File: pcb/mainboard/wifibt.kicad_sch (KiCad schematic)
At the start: 11 parts, among them U901 RTL8723BS

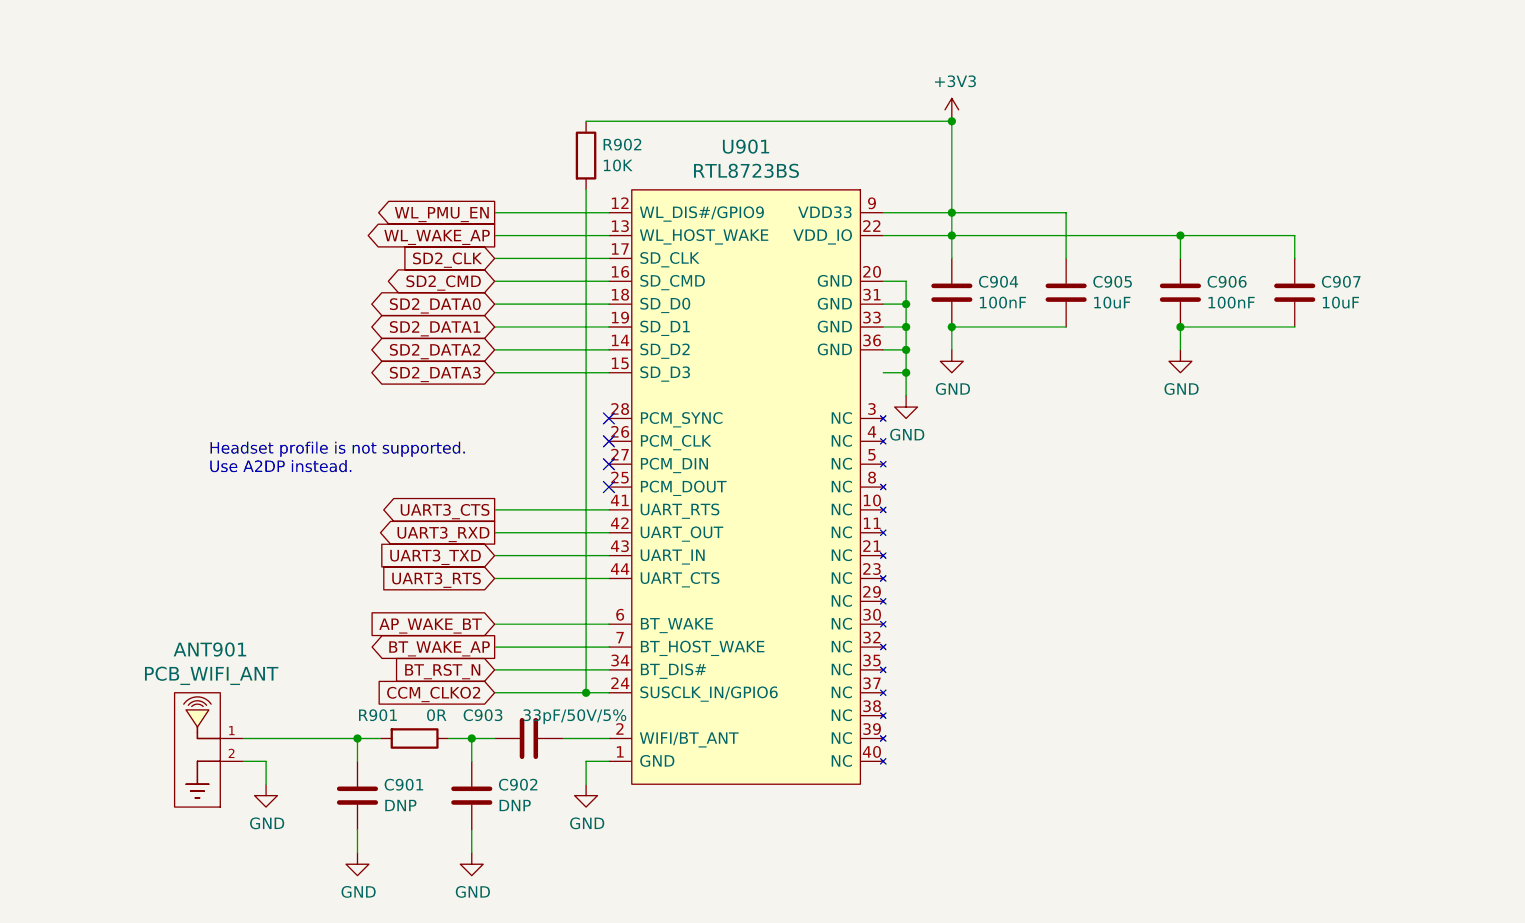
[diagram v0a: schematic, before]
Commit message: pcb: preliminary r0p1 schematics
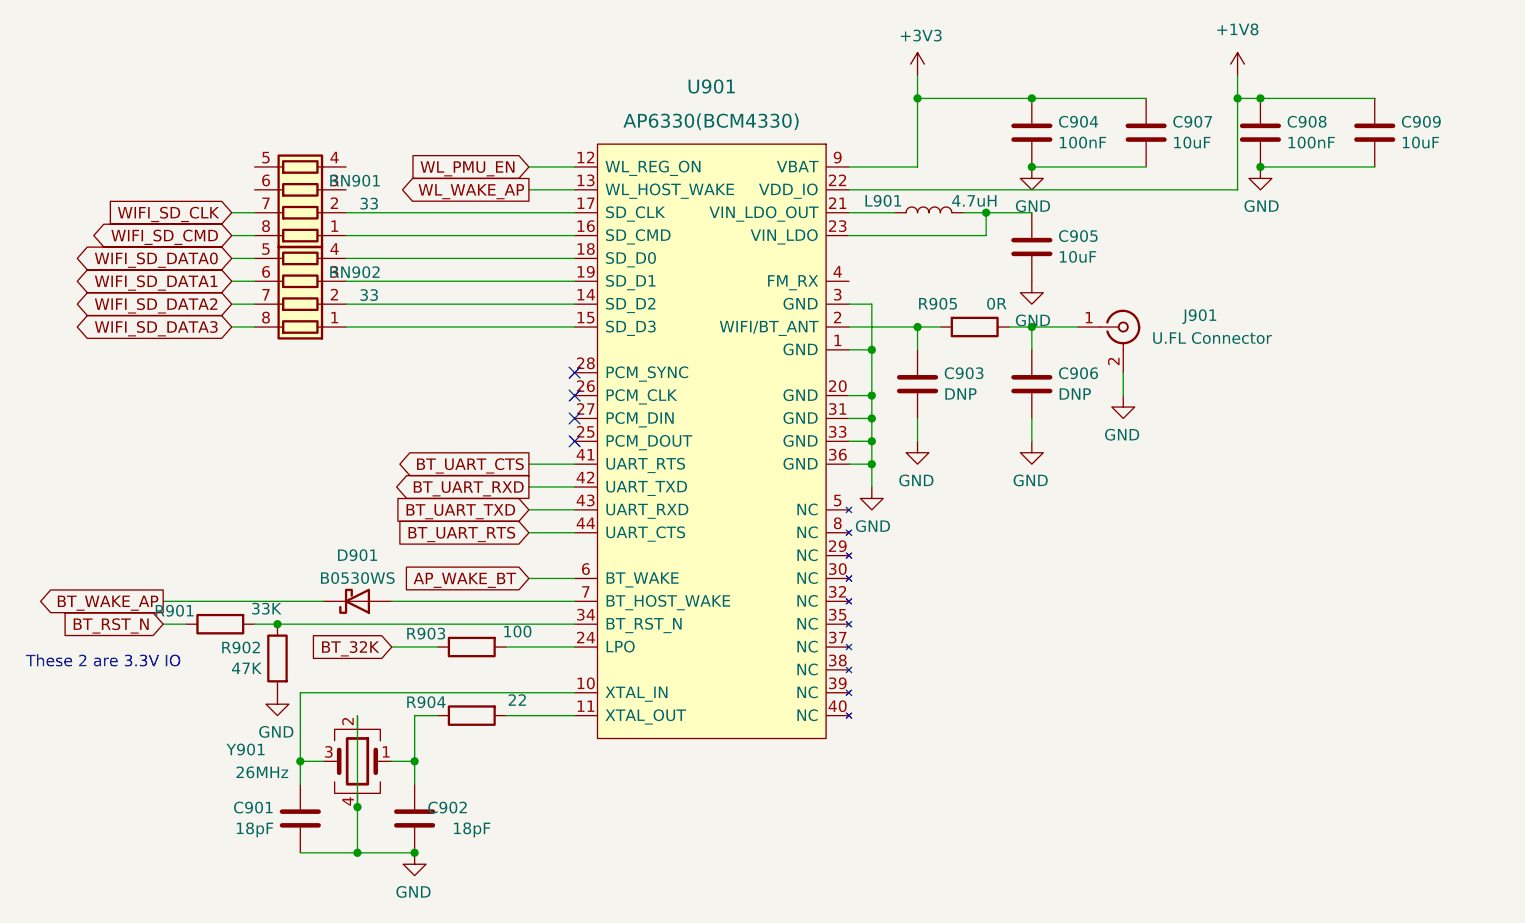
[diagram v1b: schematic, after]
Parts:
- removed ANT901: PCB_WIFI_ANT, footprints:bt_antenna_1ant_2gnd, symbol symbols:WIFI_ANT_ESP8266
- removed U901: RTL8723BS, footprints:RL-SM02BD(RTL8723BS), symbol symbols:RTL8723BS
- added C908: 100nF, Capacitor_SMD:C_0402_1005Metric, symbol Device:C
- added C909: 10uF, Capacitor_SMD:C_0603_1608Metric, symbol Device:C
- added D901: B0530WS, Diode_SMD:D_SOD-323, symbol Device:D_Schottky
- added J901: U.FL Connector, Connector_Coaxial:U.FL_Molex_MCRF_73412-0110_Vertical, symbol Connector:Conn_Coaxial
- added L901: 4.7uH, footprints:L_1212, symbol Device:L
- added R903: 100, Resistor_SMD:R_0402_1005Metric, symbol Device:R
- added R904: 22, Resistor_SMD:R_0402_1005Metric, symbol Device:R
- added R905: 0R, Resistor_SMD:R_0402_1005Metric, symbol Device:R
- added RN901, RN902: 33, Resistor_SMD:R_Array_Convex_4x0402, symbol Device:R_Pack04
- added U901: AP6330(BCM4330), footprints:RL-SM02BD(RTL8723BS), symbol symbols:AP6330(BCM4330)
- added Y901: 26MHz, Oscillator:Oscillator_SMD_Abracon_ASE-4Pin_3.2x2.5mm, symbol Device:Crystal_GND24
- C901, C902: value DNP -> 18pF
- C903: value 33pF/50V/5% -> DNP
- C906: value 100nF -> DNP
- R901: value 0R -> 33K
- R902: value 10K -> 47K
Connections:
- net CCM_CLKO2 is gone; now on net GND: R902.2
- net +3V3: now also U901.9 (VBAT); no longer C905.1, C906.1, R902.1
- net AP_WAKE_BT: now also U901.6 (BT_WAKE)
- net BT_RST_N: now also R901.1
- net BT_WAKE_AP: now also D901.1 (K)
- net GND: now also C901.2, C902.2, C903.1, C906.1, C908.2, C909.2, J901.2 (Ext), U901.1 (GND), U901.20 (GND), U901.3 (GND), U901.31 (GND), U901.33 (GND), U901.36 (GND), Y901.2, Y901.4; no longer C901.1, C902.1, C906.2
- net WL_PMU_EN: now also U901.12 (WL_REG_ON)
- net WL_WAKE_AP: now also U901.13 (WL_HOST_WAKE)
- net at R901.2: now also R902.1, U901.34 (BT_RST_N); no longer C901.2
- new net: RN902.1 (R1.1), U901.15 (SD_D3)
- new net: RN902.2 (R2.1), U901.14 (SD_D2)
- new net: RN902.3 (R3.1), U901.19 (SD_D1)
- new net: RN902.4 (R4.1), U901.18 (SD_D0)
- new net: C906.2, J901.1 (In), R905.1
- new net: C905.1, L901.2, U901.23 (VIN_LDO)
- new net: RN901.1 (R1.1), U901.16 (SD_CMD)
- new net: RN901.2 (R2.1), U901.17 (SD_CLK)
- new net: L901.1, U901.21 (VIN_LDO_OUT)
- new net: D901.2 (A), U901.7 (BT_HOST_WAKE)
- new net: C901.1, U901.10 (XTAL_IN), Y901.3
- new net: R903.2, U901.24 (LPO)
- new net: C902.1, R904.1, Y901.1
- new net: C903.2, R905.2, U901.2 (WIFI/BT_ANT)
- new net: R904.2, U901.11 (XTAL_OUT)
- new net +1V8: C908.1, C909.1, U901.22 (VDD_IO)
- new net BT_32K: R903.1
- new net BT_UART_CTS: U901.41 (UART_RTS)
- new net BT_UART_RTS: U901.44 (UART_CTS)
- new net BT_UART_RXD: U901.42 (UART_TXD)
- new net BT_UART_TXD: U901.43 (UART_RXD)
- new net WIFI_SD_CLK: RN901.7 (R2.2)
- new net WIFI_SD_CMD: RN901.8 (R1.2)
- new net WIFI_SD_DATA0: RN902.5 (R4.2)
- new net WIFI_SD_DATA1: RN902.6 (R3.2)
- new net WIFI_SD_DATA2: RN902.7 (R2.2)
- new net WIFI_SD_DATA3: RN902.8 (R1.2)
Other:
- note added: "These 2 are 3.3V IO"
- note removed: "Headset profile is not supported. Use A2DP instead."
- company: Copyright EI-2030 2021. / Engineer: Wenting Zhang -> Copyright Modos 2021. / Engineer: Wenting Zhang

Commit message: pcb: initial placement for mb
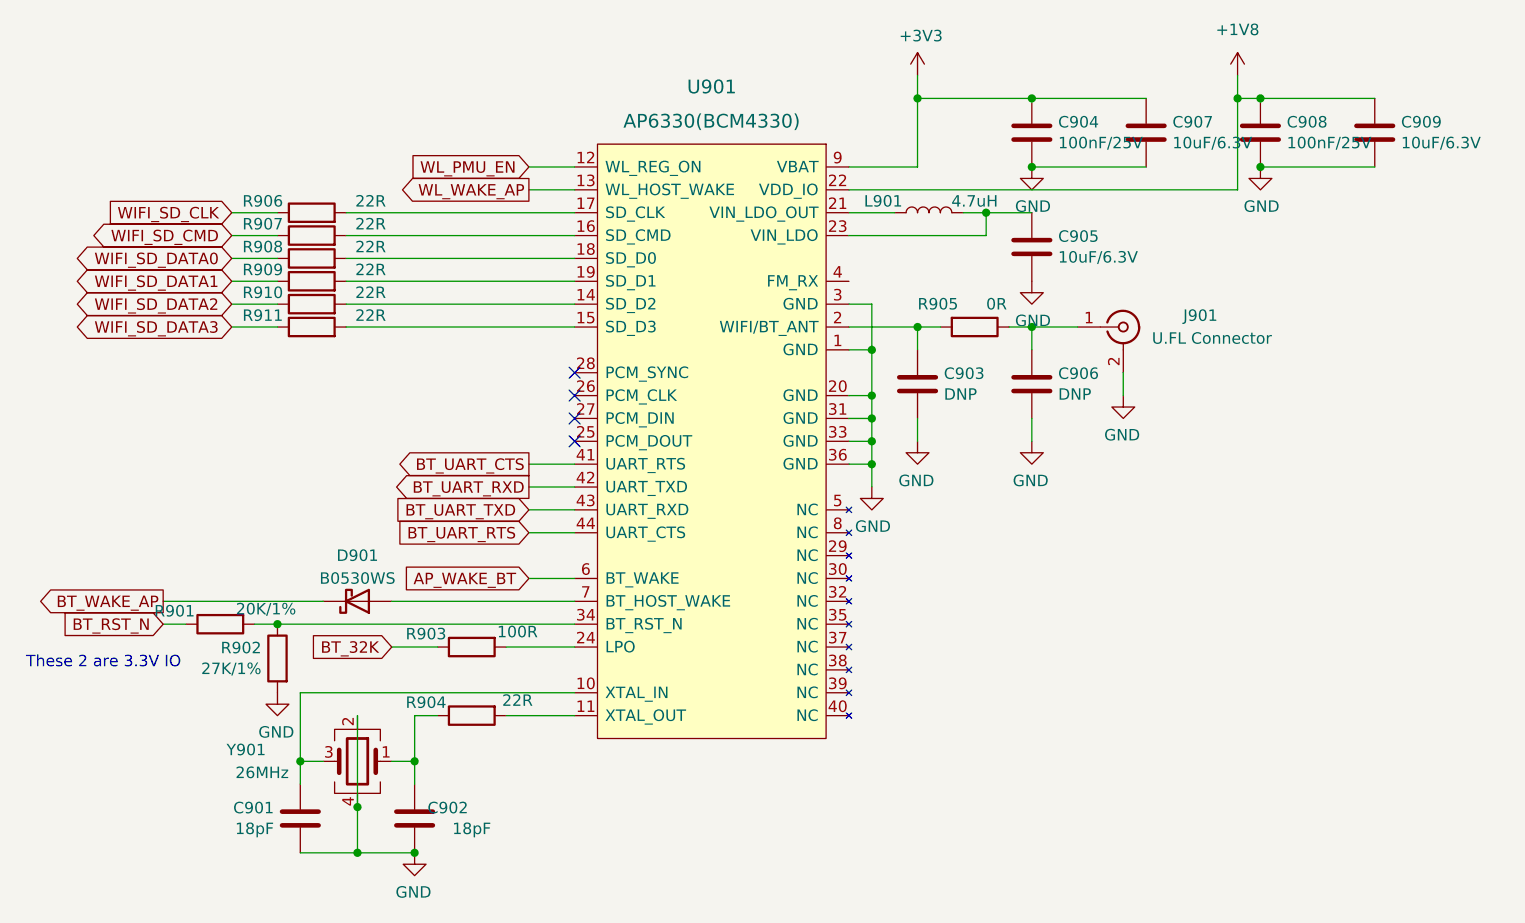
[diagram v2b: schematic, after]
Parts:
- removed RN901, RN902: 33, Resistor_SMD:R_Array_Convex_4x0402, symbol Device:R_Pack04
- added R906, R907, R908, R909, R910, R911: 22R, Resistor_SMD:R_0402_1005Metric, symbol Device:R
- C901, C902: LCSC (none) -> C182481; Ref.Price (none) -> 0.0061
- C903, C906: LCSC (none) -> -; Ref.Price (none) -> 0
- C904, C908: value 100nF -> 100nF/25V; LCSC (none) -> C56392; Ref.Price (none) -> 0.0023
- C905, C907, C909: value 10uF -> 10uF/6.3V; LCSC (none) -> C105490; Ref.Price (none) -> 0.0165
- D901: LCSC (none) -> C475612; Ref.Price (none) -> 0.0209
- J901: LCSC (none) -> C88374; Ref.Price (none) -> 0.0897
- L901: LCSC (none) -> C340379; Ref.Price (none) -> 0.0643
- R901: value 33K -> 20K/1%; LCSC (none) -> C93942; Ref.Price (none) -> 0.0011
- R902: value 47K -> 27K/1%; LCSC (none) -> C138022; Ref.Price (none) -> 0.0029
- R903: value 100 -> 100R; LCSC (none) -> C106233; Ref.Price (none) -> 0.0007
- R904: value 22 -> 22R; LCSC (none) -> C93929; Ref.Price (none) -> 0.002
- R905: LCSC (none) -> C60485; Ref.Price (none) -> 0.0008
- U901: Ref.Price (none) -> 3.04
- Y901: footprint Oscillator:Oscillator_SMD_Abracon_ASE-4Pin_3.2x2.5mm -> Crystal:Crystal_SMD_3225-4Pin_3.2x2.5mm; LCSC (none) -> C390775; Ref.Price (none) -> 0.1123
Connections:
- net WIFI_SD_CLK: now also R906.1
- net WIFI_SD_CMD: now also R907.1
- net WIFI_SD_DATA0: now also R908.1
- net WIFI_SD_DATA1: now also R909.1
- net WIFI_SD_DATA2: now also R910.1
- net WIFI_SD_DATA3: now also R911.1
- net at U901.15 (SD_D3): now also R911.2
- net at U901.14 (SD_D2): now also R910.2
- net at U901.19 (SD_D1): now also R909.2
- net at U901.18 (SD_D0): now also R908.2
- net at U901.16 (SD_CMD): now also R907.2
- net at U901.17 (SD_CLK): now also R906.2
